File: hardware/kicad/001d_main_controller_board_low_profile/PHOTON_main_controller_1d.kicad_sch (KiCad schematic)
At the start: 65 parts, among them J101 JST_SH, J102 JST_SH RS-485_1, J103 JST_SH RS-485_2, J104 JST_SH RS-485_2, J3 USB_C_Receptacle_USB2.0, J4 Micro_SD_Card, U1 RP2354_60QFN, U102 THVD1424RGTR, U4 TPD4E05U06DQAR, U5 TPS62A0569ADRLR, Y1 ABM8-272-T3

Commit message: 002 sensor board: 5V bus rework, library consolidation, DRC pass
Board (002):
- Remove SS14 bridging diode; USB-C VBUS and JST V+ are now one net.
  Worst case is back-powering a host's VBUS, acceptable in a uniform
  5V fleet, and it drops 185mW in the bridging case.
- Remove the 8x 47k CS pull-ups. At 47k they parked the TLA2518 CS
  inputs mid-rail (1.7-2.1V, between VIL 0.99 and VIH 2.31); the
  internal pull-down now defines them cleanly low. Firmware must drive
  CS high before configuring SPI.
- 5V pour along the bottom edge, 3.3V moved up to the mounting rail.
- USB-C relocated; ~200mm D+/D- run on F.Cu over the B.Cu GND pour.
- Screw-head keepouts on all mounting holes.
- Board grown 2mm in Y -> 413.66 x 35.00 mm.

Net classes:
- USB_DIFF_90 -> USB_FS, diff pair 0.8/0.15 -> 0.35/0.15. The old name
  claimed 90 ohm; on a 1.51mm 2-layer stackup it is ~140 ohm and cannot
  be otherwise. Irrelevant at Full Speed.
- Add PWR_5V (+5V) and RS485 (/RS485_P, /RS485_N).
- Restore the +3V3 -> VCC assignment lost during the rename.

Libraries:
- footprints/ -> footprints.pretty/ so KiCad will save into it.
- Consolidate symbols into PHOTON / PHOTON_Modified on 001d and 002;
  drop unused vendor-exported libraries.
- Add mousebite_34mm: 17x 1.2mm NPTH at 2mm pitch. 0.8mm webs cut more
  easily than the old 1.4mm and still pass a 0.3mm trace.
- Fix MountingHole_2.7mm_M2.5_Keepout: it disallowed pads, so each hole
  flagged its own NPTH (17 DRC errors).

Fab outputs now tracked via .gitignore negation for production/*.csv.

Co-Authored-By: Claude Opus 5 <noreply@anthropic.com>
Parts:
- CR1, CR2, CR5: symbol 2025-08-11_08-49-29:SMF5.0A -> PHOTON:SMF5.0A
- J3: symbol Connector:USB_C_Receptacle_USB2.0 -> PHOTON_Modified:USB_C_Receptacle_USB2.0
- J4: footprint Pretty Custom:TF-015_corrected -> footprints:TF-015_corrected; symbol Connector:Micro_SD_Card -> PHOTON_Modified:Micro_SD_Card
- U1: symbol MCU_RaspberryPi_RP2350:RP2350_60QFN -> PHOTON:RP2350_60QFN
- U102: footprint Pretty Custom:QFN_24RGTR_TEX -> footprints:QFN_24RGTR_TEX; symbol 2025-11-21_08-29-10_THVD1424RGTR:THVD1424RGTR -> PHOTON:THVD1424RGTR
- U4: symbol 2025-08-11_08-44-22:TPD4E05U06QDQARQ1 -> PHOTON:TPD4E05U06QDQARQ1
- U5: footprint Pretty Custom:DRL0006A-MFG -> footprints:SOT-563_DRL0006A; symbol TI BUCK:TPS62A0569ADRLR -> PHOTON:TPS62A0569ADRLR
- Y1: symbol Device:Crystal_GND24 -> PHOTON_Modified:Crystal_GND24
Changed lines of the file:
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@@
 	)
 	(symbol
-		(lib_id "2025-08-11_08-49-29:SMF5.0A")
+		(lib_id "PHOTON:SMF5.0A")
 		(at 58.42 218.44 180)
 		(unit 1)
@@
 	)
 	(symbol
-		(lib_id "2025-08-11_08-44-22:TPD4E05U06QDQARQ1")
+		(lib_id "PHOTON:TPD4E05U06QDQARQ1")
 		(at 67.31 262.89 0)
 		(unit 1)
@@
 	)
 	(symbol
-		(lib_id "TI BUCK:TPS62A0569ADRLR")
+		(lib_id "PHOTON:TPS62A0569ADRLR")
 		(at 137.16 223.52 0)
 		(unit 1)
@@
 			)
 		)
-		(property "Footprint" "Pretty Custom:DRL0006A-MFG"
+		(property "Footprint" "footprints:SOT-563_DRL0006A"
 			(at 137.16 223.52 0)
 			(hide yes)
@@
 	)
 	(symbol
-		(lib_id "Connector:Micro_SD_Card")
+		(lib_id "PHOTON_Modified:Micro_SD_Card")
 		(at 289.56 184.15 0)
 		(unit 1)
@@
 			)
 		)
-		(property "Footprint" "Pretty Custom:TF-015_corrected"
+		(property "Footprint" "footprints:TF-015_corrected"
 			(at 318.77 176.53 0)
 			(hide yes)
@@
 	)
 	(symbol
-		(lib_id "Connector:USB_C_Receptacle_USB2.0")
+		(lib_id "PHOTON_Modified:USB_C_Receptacle_USB2.0")
 		(at 27.94 238.76 0)
 		(unit 1)
@@
 	)
 	(symbol
-		(lib_id "2025-08-11_08-49-29:SMF5.0A")
+		(lib_id "PHOTON:SMF5.0A")
 		(at 58.42 91.44 0)
 		(mirror y)
@@
 	)
 	(symbol
-		(lib_id "MCU_RaspberryPi_RP2350:RP2350_60QFN")
+		(lib_id "PHOTON:RP2350_60QFN")
 		(at 280.67 104.14 0)
 		(unit 1)
@@
 	)
 	(symbol
-		(lib_id "2025-08-11_08-49-29:SMF5.0A")
+		(lib_id "PHOTON:SMF5.0A")
 		(at 46.99 148.59 180)
 		(unit 1)
@@
 	)
 	(symbol
-		(lib_id "Device:Crystal_GND24")
+		(lib_id "PHOTON_Modified:Crystal_GND24")
 		(at 355.6 236.22 270)
 		(unit 1)
@@
 	)
 	(symbol
-		(lib_id "2025-11-21_08-29-10_THVD1424RGTR:THVD1424RGTR")
+		(lib_id "PHOTON:THVD1424RGTR")
 		(at 100.33 160.02 0)
 		(unit 1)
@@
 			)
 		)
-		(property "Footprint" "Pretty Custom:QFN_24RGTR_TEX"
+		(property "Footprint" "footprints:QFN_24RGTR_TEX"
 			(at 100.33 160.02 0)
 			(hide yes)

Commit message: Consolidate footprints into a single shared library
All three boards carried their own copies of the same footprints - 79
files across 11 project libraries for 37 distinct footprints. Several
existed three times over (RP2350-QFN-60 ThermalVias, edge_holes,
TO-236_VIS-L, SON_NT2020_VIS, L_pol_2016, USB_Micro-B). Three copies
drift, and this project has already been bitten twice by a library and
a board disagreeing.

- New hardware/kicad/common.pretty holds all 37, verified byte-identical
  where they were duplicated: zero name collisions with differing
  content, so nothing had to be reconciled.
- Each board's fp-lib-table is now a single "common" entry. Previously
  001 alone had eight, and the nickname "footprints" meant a different
  library on each of the three boards - so lib_ids were rewritten per
  board, not globally.
- 459 footprint references across the three boards now resolve. That
  includes SparkFun-Qwiic:qwiic_8mm on 001, which was referenced but
  had never been in any fp-lib-table - broken before this change.

Also shrinks docs/images/reflective_sensor.png from 2816x1536 / 4.43 MB
to 1600x873 / 1.72 MB.

Co-Authored-By: Claude Opus 5 <noreply@anthropic.com>
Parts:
- C2, C3: footprint RP2350_60QFN_minimal:C_0402_1005Metric_small_pads -> common:C_0402_1005Metric_small_pads
- J4: footprint footprints:TF-015_corrected -> common:TF-015_corrected
- L1: footprint RP2350_60QFN_minimal:L_pol_2016 -> common:L_pol_2016
- U1: footprint RP2350_60QFN_minimal:RP2350-QFN-60-1EP_7x7_P0.4mm_EP3.4x3.4mm_ThermalVias -> common:RP2350-QFN-60-1EP_7x7_P0.4mm_EP3.4x3.4mm_ThermalVias
- U102: footprint footprints:QFN_24RGTR_TEX -> common:QFN_24RGTR_TEX
- U4: footprint footprints:DQA0010A -> common:DQA0010A
- U5: footprint footprints:SOT-563_DRL0006A -> common:SOT-563_DRL0006A
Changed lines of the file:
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@@
 			)
 		)
-		(property "Footprint" "footprints:DQA0010A"
+		(property "Footprint" "common:DQA0010A"
 			(at 67.31 262.89 0)
 			(hide yes)
@@
 			)
 		)
-		(property "Footprint" "footprints:SOT-563_DRL0006A"
+		(property "Footprint" "common:SOT-563_DRL0006A"
 			(at 137.16 223.52 0)
 			(hide yes)
@@
 			)
 		)
-		(property "Footprint" "footprints:TF-015_corrected"
+		(property "Footprint" "common:TF-015_corrected"
 			(at 318.77 176.53 0)
 			(hide yes)
@@
 			)
 		)
-		(property "Footprint" "RP2350_60QFN_minimal:C_0402_1005Metric_small_pads"
+		(property "Footprint" "common:C_0402_1005Metric_small_pads"
 			(at 191.4652 71.12 0)
 			(hide yes)
@@
 			)
 		)
-		(property "Footprint" "RP2350_60QFN_minimal:RP2350-QFN-60-1EP_7x7_P0.4mm_EP3.4x3.4mm_ThermalVias"
+		(property "Footprint" "common:RP2350-QFN-60-1EP_7x7_P0.4mm_EP3.4x3.4mm_ThermalVias"
 			(at 261.62 104.14 0)
 			(hide yes)
@@
 			)
 		)
-		(property "Footprint" "RP2350_60QFN_minimal:L_pol_2016"
+		(property "Footprint" "common:L_pol_2016"
 			(at 217.17 67.31 0)
 			(hide yes)
@@
 			)
 		)
-		(property "Footprint" "footprints:QFN_24RGTR_TEX"
+		(property "Footprint" "common:QFN_24RGTR_TEX"
 			(at 100.33 160.02 0)
 			(hide yes)
@@
 			)
 		)
-		(property "Footprint" "RP2350_60QFN_minimal:C_0402_1005Metric_small_pads"
+		(property "Footprint" "common:C_0402_1005Metric_small_pads"
 			(at 202.8952 71.12 0)
 			(hide yes)

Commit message: Rename shared footprint library common -> photon_common
'common' is too generic for a library nickname - it can collide with a
global library or another project's table, and it doesn't identify whose
footprints these are.

155 lib_ids rewritten across the three boards plus all three
fp-lib-tables. All 459 footprint references still resolve.

Co-Authored-By: Claude Opus 5 <noreply@anthropic.com>
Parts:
- C2, C3: footprint common:C_0402_1005Metric_small_pads -> photon_common:C_0402_1005Metric_small_pads
- J4: footprint common:TF-015_corrected -> photon_common:TF-015_corrected
- L1: footprint common:L_pol_2016 -> photon_common:L_pol_2016
- U1: footprint common:RP2350-QFN-60-1EP_7x7_P0.4mm_EP3.4x3.4mm_ThermalVias -> photon_common:RP2350-QFN-60-1EP_7x7_P0.4mm_EP3.4x3.4mm_ThermalVias
- U102: footprint common:QFN_24RGTR_TEX -> photon_common:QFN_24RGTR_TEX
- U4: footprint common:DQA0010A -> photon_common:DQA0010A
- U5: footprint common:SOT-563_DRL0006A -> photon_common:SOT-563_DRL0006A
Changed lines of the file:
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@@
 			)
 		)
-		(property "Footprint" "common:DQA0010A"
+		(property "Footprint" "photon_common:DQA0010A"
 			(at 67.31 262.89 0)
 			(hide yes)
@@
 			)
 		)
-		(property "Footprint" "common:SOT-563_DRL0006A"
+		(property "Footprint" "photon_common:SOT-563_DRL0006A"
 			(at 137.16 223.52 0)
 			(hide yes)
@@
 			)
 		)
-		(property "Footprint" "common:TF-015_corrected"
+		(property "Footprint" "photon_common:TF-015_corrected"
 			(at 318.77 176.53 0)
 			(hide yes)
@@
 			)
 		)
-		(property "Footprint" "common:C_0402_1005Metric_small_pads"
+		(property "Footprint" "photon_common:C_0402_1005Metric_small_pads"
 			(at 191.4652 71.12 0)
 			(hide yes)
@@
 			)
 		)
-		(property "Footprint" "common:RP2350-QFN-60-1EP_7x7_P0.4mm_EP3.4x3.4mm_ThermalVias"
+		(property "Footprint" "photon_common:RP2350-QFN-60-1EP_7x7_P0.4mm_EP3.4x3.4mm_ThermalVias"
 			(at 261.62 104.14 0)
 			(hide yes)
@@
 			)
 		)
-		(property "Footprint" "common:L_pol_2016"
+		(property "Footprint" "photon_common:L_pol_2016"
 			(at 217.17 67.31 0)
 			(hide yes)
@@
 			)
 		)
-		(property "Footprint" "common:QFN_24RGTR_TEX"
+		(property "Footprint" "photon_common:QFN_24RGTR_TEX"
 			(at 100.33 160.02 0)
 			(hide yes)
@@
 			)
 		)
-		(property "Footprint" "common:C_0402_1005Metric_small_pads"
+		(property "Footprint" "photon_common:C_0402_1005Metric_small_pads"
 			(at 202.8952 71.12 0)
 			(hide yes)

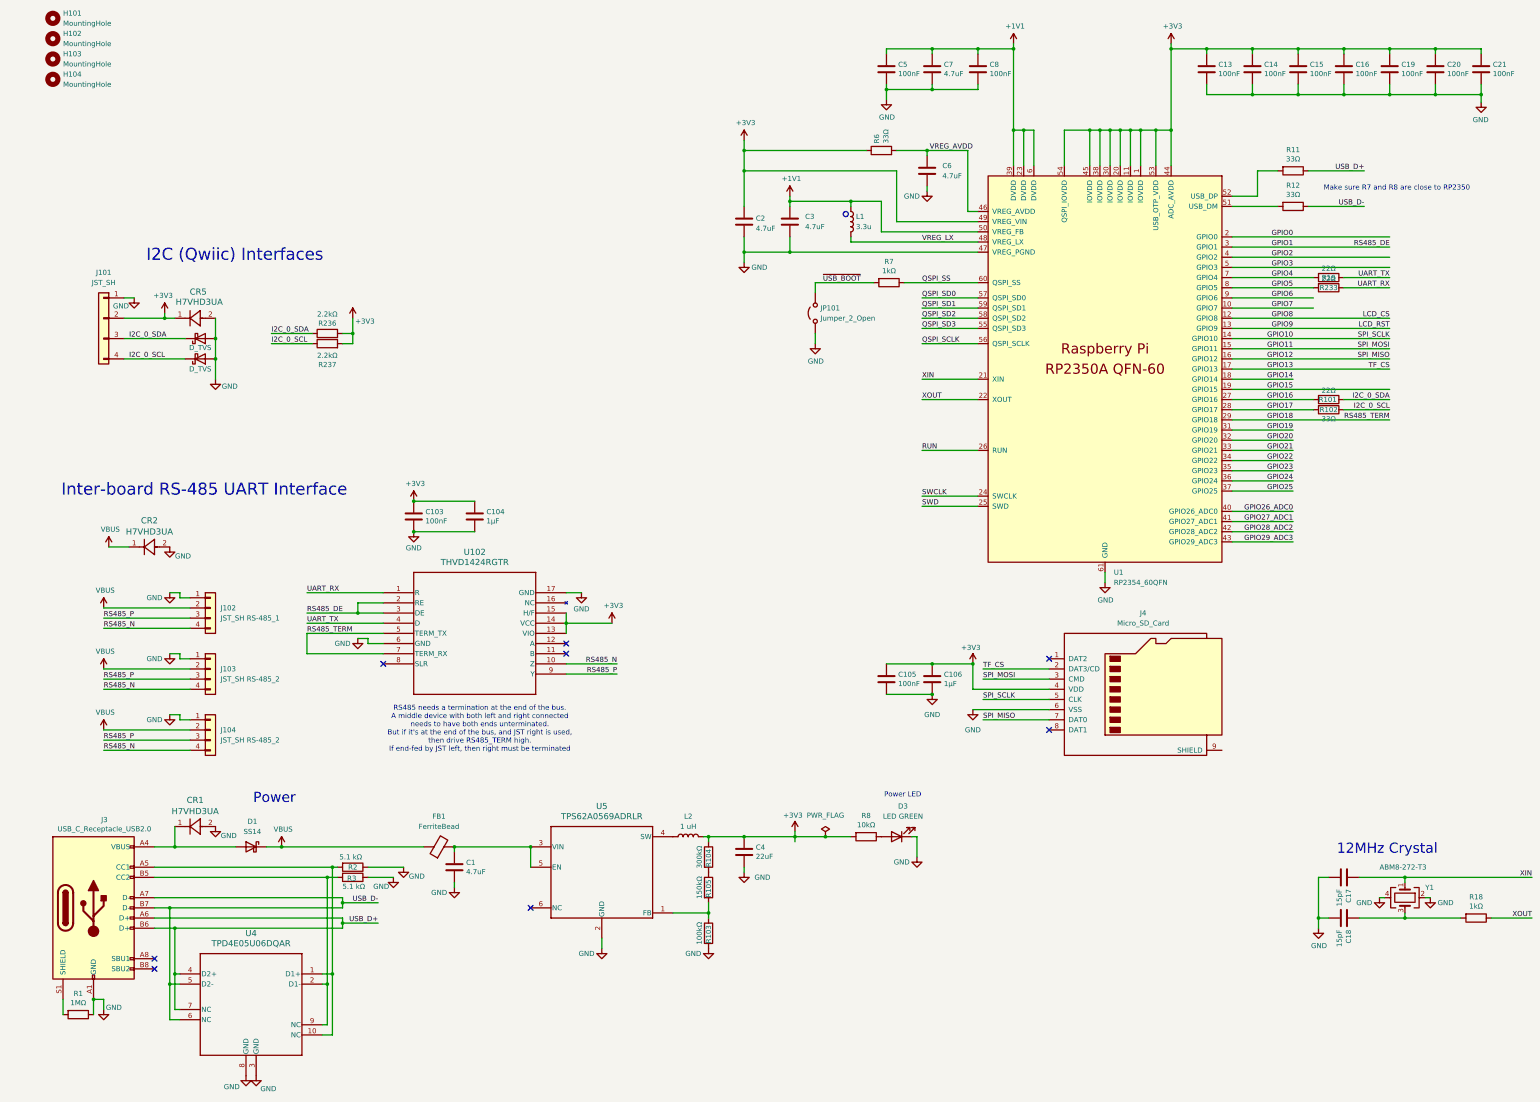
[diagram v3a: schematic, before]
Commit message: Consolidate symbol libraries, normalise BOM data, Rev B for all three boards
Libraries
- Move PHOTON and PHOTON_Modified to hardware/kicad/, shared by all three
  projects, replacing six divergent per-project copies. 002's versions taken
  as canonical (correct pin electrical types); 001-only parts recovered from
  the schematic cache. All 459 footprint and 464 symbol refs resolve.
- Repoint every sym-lib-table at the shared files. Nicknames unchanged, so
  002 and 001d needed no lib_id edits; only 001's stale date-named ones.
- Fix stale footprint nicknames inside the symbol libraries (footprints:,
  RP2350_60QFN_minimal:, APS6404L-3SQR-ZR:) that would have made newly
  placed parts land with unresolvable footprints.
- Reset baked-in reference designators and MPNs on six library footprints
  back to REF** and the footprint name. SOT-563_DRL0006A carried "U6",
  which would have overwritten 001d's U5 on any field-resetting update.

Footprints
- Add SON-8_3x2mm_P0.5mm: KiCad stock SON-8 with the exposed pad and its
  four paste apertures removed. The APS6404L USON-8L (JEDEC MO-229) has no
  thermal pad and 0-0.05mm standoff, so both the copper and the paste under
  the body were wrong. Replaces the easyeda2kicad footprint on U101, whose
  0.102mm mask margin also bridged all six 0.5mm-pitch mask openings.
- Mounting holes on 001 and 001d move to the photon_common keepout
  footprint, matching 002, so a screw head cannot bridge the F.Cu power
  pour to the B.Cu ground pour.
- Remove the unused TDK T3902 microphone footprint.

BOM
- Normalise values fleet-wide: Greek mu -> ascii u, strip spaces before
  units, complete truncated inductor values. Each was splitting one part
  into two BOM lines, since the fab toolkit groups on footprint+value.
- Unify JST-SH connector values so each board emits one line, not three.
  Per-connector labels moved to Description, which is not a BOM column.
- Assign part numbers to the four largest passive lines: 100nF C1525,
  1uF C52923, 1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
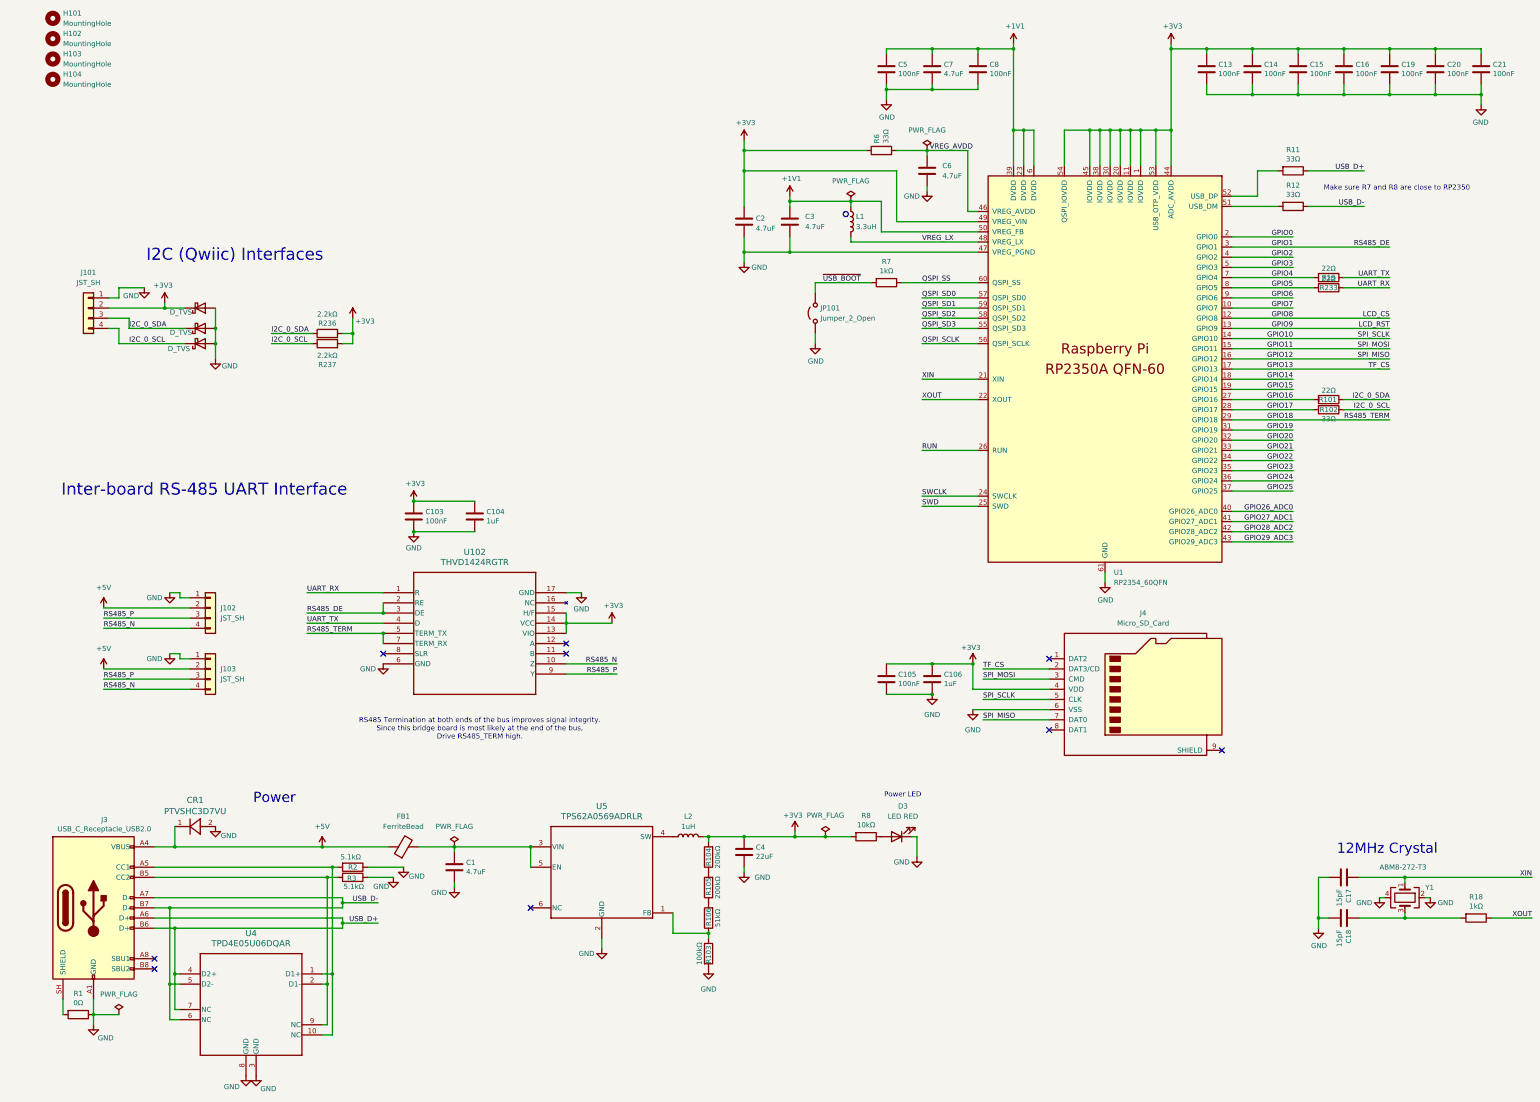
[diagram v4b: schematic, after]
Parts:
- removed CR2, CR5: H7VHD3UA, Diode_SMD:D_SOD-323, symbol PHOTON:SMF5.0A
- removed D1: SS14, Diode_SMD:D_SMA, symbol Device:D_Schottky
- removed J104: JST_SH RS-485_2, Connector_JST:JST_SH_SM04B-SRSS-TB_1x04-1MP_P1.00mm_Horizontal, symbol Connector_Generic:Conn_01x04
- added D12: D_TVS, Diode_SMD:D_SOD-523, symbol Device:D_Schottky
- added R106: 51kΩ, Resistor_SMD:R_0402_1005Metric, symbol Device:R
- C103, C105, C13, C14, C15, C16, C19, C20, C21, C5, C8: JLCPCB Part # (none) -> C1525
- C104, C106: value 1μF -> 1uF; JLCPCB Part # (none) -> C52923
- C17, C18: JLCPCB Part # (none) -> C1548
- CR1: value H7VHD3UA -> PTVSHC3D7VU; footprint Diode_SMD:D_SOD-323 -> photon_common:SOD-323_L1.8-W1.3-LS2.5-RD
- D3: value LED GREEN -> LED RED; footprint LED_SMD:LED_0402_1005Metric -> LED_SMD:LED_0603_1608Metric; JLCPCB Part # C130722 -> C2286
- H101, H102, H103, H104: footprint MountingHole:MountingHole_2.7mm_M2.5_ISO7380 -> photon_common:MountingHole_2.7mm_M2.5_Keepout
- J102: value JST_SH RS-485_1 -> JST_SH
- J103: value JST_SH RS-485_2 -> JST_SH
- L1: value 3.3u -> 3.3uH
- L2: value 1 uH -> 1uH
- R1: value 1MΩ -> 0Ω; footprint Resistor_SMD:R_0805_2012Metric_Pad1.20x1.40mm_HandSolder -> Resistor_SMD:R_0402_1005Metric
- R104: value 300kΩ -> 200kΩ
- R105: value 150kΩ -> 200kΩ
- R2, R3: value 5.1 kΩ -> 5.1kΩ
- U102: JLCPCB Part # (none) -> C5359161
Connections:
- net +3V3: now also R104.2, D12.1 (K); no longer R104.1
- net GND: now also D12.2 (A)
- net at R103.1, U5.1 (FB): now also R106.1; no longer R105.2
- net at R1.2: now also J3.SH (SHIELD); no longer J3.S1 (SHIELD)
- net at R105.1: now also R106.2; no longer R104.2
- net VBUS renamed +5V
- new net: R104.1, R105.2
- no-connect marks 8 -> 9
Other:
- note added: "RS485 Termination at both ends of the bus improves signal integrity. Since this bridge board is most likely at the end of the bus, Drive RS485_TERM high."
- note removed: "RS485 needs a termination at the end of the bus. A middle device with both left and right connected needs to have both ends unterminated. But if it's at the end of the bus, and JST right is used, then drive RS485_TERM high. If end-fed by JST left, then right must be terminated"
- moved on the sheet: FB1, J101, R7
